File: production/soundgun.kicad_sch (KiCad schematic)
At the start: 16 parts, among them J1 STX-3000, J3 Screw_Terminal_01x02, J4 Screw_Terminal_01x02, U1 LM358, U2 MIC4427, U3 Pico

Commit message: Cleaned Release project
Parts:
- removed J4: Screw_Terminal_01x02, TerminalBlock_Phoenix:TerminalBlock_Phoenix_PT-1,5-2-3.5-H_1x02_P3.50mm_Horizontal, symbol Connector:Screw_Terminal_01x02
- renumbered C6 to C1, D3 to D1, J3 to J2, R4 to R1, R8 to R2, R10 to R3, R9 to R4, R1 to R5
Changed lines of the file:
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@@
 		(dnp no)
 		(fields_autoplaced yes)
-		(property "Reference" "R9"
+		(property "Reference" "R4"
 			(at 140.97 152.4 90)
 			(effects
@@
 			(project "soundgun"
 				(path "/09bb77e0-3bf3-4c24-ad5d-31155c7bb1e6"
-					(reference "R9")
+					(reference "R4")
 					(unit 1)
 				)
@@
 		(dnp no)
 		(fields_autoplaced yes)
-		(property "Reference" "#PWR016"
+		(property "Reference" "#PWR07"
 			(at 273.05 165.1 0)
 			(effects
@@
 			(project "soundgun"
 				(path "/09bb77e0-3bf3-4c24-ad5d-31155c7bb1e6"
-					(reference "#PWR016")
+					(reference "#PWR07")
 					(unit 1)
 				)
@@
 		(dnp no)
 		(fields_autoplaced yes)
-		(property "Reference" "C6"
+		(property "Reference" "C1"
 			(at 105.41 182.8799 0)
 			(effects
@@
 			(project "soundgun"
 				(path "/09bb77e0-3bf3-4c24-ad5d-31155c7bb1e6"
-					(reference "C6")
+					(reference "C1")
 					(unit 1)
 				)
@@
 		(dnp no)
 		(fields_autoplaced yes)
-		(property "Reference" "#PWR025"
+		(property "Reference" "#PWR01"
 			(at 35.56 151.13 0)
 			(effects
@@
 			(project "soundgun"
 				(path "/09bb77e0-3bf3-4c24-ad5d-31155c7bb1e6"
-					(reference "#PWR025")
+					(reference "#PWR01")
 					(unit 1)
 				)
@@
 		(on_board yes)
 		(dnp no)
-		(property "Reference" "#PWR09"
+		(property "Reference" "#PWR05"
 			(at 55.88 152.4 0)
 			(effects
@@
 			(project "soundgun"
 				(path "/09bb77e0-3bf3-4c24-ad5d-31155c7bb1e6"
-					(reference "#PWR09")
+					(reference "#PWR05")
 					(unit 1)
 				)
@@
 		(dnp no)
 		(fields_autoplaced yes)
-		(property "Reference" "R8"
+		(property "Reference" "R2"
 			(at 127 152.4 90)
 			(effects
@@
 			(project "soundgun"
 				(path "/09bb77e0-3bf3-4c24-ad5d-31155c7bb1e6"
-					(reference "R8")
+					(reference "R2")
 					(unit 1)
 				)
@@
 		(dnp no)
 		(fields_autoplaced yes)
-		(property "Reference" "#PWR02"
+		(property "Reference" "#PWR06"
 			(at 80.01 129.54 0)
 			(effects
@@
 			(project "soundgun"
 				(path "/09bb77e0-3bf3-4c24-ad5d-31155c7bb1e6"
-					(reference "#PWR02")
+					(reference "#PWR06")
 					(unit 1)
 				)
@@
 		(dnp no)
 		(fields_autoplaced yes)
-		(property "Reference" "R4"
+		(property "Reference" "R1"
 			(at 110.49 160.0199 0)
 			(effects
@@
 			(project "soundgun"
 				(path "/09bb77e0-3bf3-4c24-ad5d-31155c7bb1e6"
-					(reference "R4")
-					(unit 1)
-				)
-			)
-		)
-	)
-	(symbol
-		(lib_id "Connector:Screw_Terminal_01x02")
-		(at 59.69 168.91 0)
-		(mirror y)
-		(unit 1)
-		(exclude_from_sim no)
-		(in_bom yes)
-		(on_board yes)
-		(dnp no)
-		(property "Reference" "J4"
-			(at 57.15 168.9099 0)
-			(effects
-				(font
-					(size 1.27 1.27)
-				)
-				(justify left)
-			)
-		)
-		(property "Value" "Screw_Terminal_01x02"
-			(at 57.15 171.4499 0)
-			(effects
-				(font
-					(size 1.27 1.27)
-				)
-				(justify left)
-			)
-		)
-		(property "Footprint" "TerminalBlock_Phoenix:TerminalBlock_Phoenix_PT-1,5-2-3.5-H_1x02_P3.50mm_Horizontal"
-			(at 59.69 168.91 0)
-			(effects
-				(font
-					(size 1.27 1.27)
-				)
-				(hide yes)
-			)
-		)
-		(property "Datasheet" "~"
-			(at 59.69 168.91 0)
-			(effects
-				(font
-					(size 1.27 1.27)
-				)
-				(hide yes)
-			)
-		)
-		(property "Description" "Generic screw terminal, single row, 01x02, script generated (kicad-library-utils/schlib/autogen/connector/)"
-			(at 59.69 168.91 0)
-			(effects
-				(font
-					(size 1.27 1.27)
-				)
-				(hide yes)
-			)
-		)
-		(pin "2"
-		)
-		(pin "1"
-		)
-		(instances
-			(project "soundgun"
-				(path "/09bb77e0-3bf3-4c24-ad5d-31155c7bb1e6"
-					(reference "J4")
+					(reference "R1")
 					(unit 1)
 				)
@@
 		(on_board yes)
 		(dnp no)
-		(property "Reference" "R1"
+		(property "Reference" "R5"
 			(at 140.97 166.624 90)
 			(effects
@@
 			(project "soundgun"
 				(path "/09bb77e0-3bf3-4c24-ad5d-31155c7bb1e6"
-					(reference "R1")
+					(reference "R5")
 					(unit 1)
 				)
@@
 		(dnp no)
 		(fields_autoplaced yes)
-		(property "Reference" "#PWR01"
+		(property "Reference" "#PWR04"
 			(at 49.53 130.81 0)
 			(effects
@@
 			(project "soundgun"
 				(path "/09bb77e0-3bf3-4c24-ad5d-31155c7bb1e6"
-					(reference "#PWR01")
+					(reference "#PWR04")
 					(unit 1)
 				)
@@
 		(dnp no)
 		(fields_autoplaced yes)
-		(property "Reference" "R10"
+		(property "Reference" "R3"
 			(at 127 163.83 90)
 			(effects
@@
 			(project "soundgun"
 				(path "/09bb77e0-3bf3-4c24-ad5d-31155c7bb1e6"
-					(reference "R10")
+					(reference "R3")
 					(unit 1)
 				)
@@
 		(dnp no)
 		(fields_autoplaced yes)
-		(property "Reference" "#FLG05"
+		(property "Reference" "#FLG01"
 			(at 25.4 168.275 0)
 			(effects
@@
 			(project "soundgun"
 				(path "/09bb77e0-3bf3-4c24-ad5d-31155c7bb1e6"
-					(reference "#FLG05")
+					(reference "#FLG01")
 					(unit 1)
 				)
@@
 		(dnp no)
 		(fields_autoplaced yes)
-		(property "Reference" "D3"
+		(property "Reference" "D1"
 			(at 157.48 176.8474 90)
 			(effects
@@
 			(project "soundgun"
 				(path "/09bb77e0-3bf3-4c24-ad5d-31155c7bb1e6"
-					(reference "D3")
+					(reference "D1")
 					(unit 1)
 				)
@@
 		(dnp no)
 		(fields_autoplaced yes)
-		(property "Reference" "#PWR010"
+		(property "Reference" "#PWR03"
 			(at 46.99 152.4 0)
 			(effects
@@
 			(project "soundgun"
 				(path "/09bb77e0-3bf3-4c24-ad5d-31155c7bb1e6"
-					(reference "#PWR010")
+					(reference "#PWR03")
 					(unit 1)
 				)
@@
 		(on_board yes)
 		(dnp no)
-		(property "Reference" "J3"
+		(property "Reference" "J2"
 			(at 251.46 133.3501 0)
 			(effects
@@
 			(project "soundgun"
 				(path "/09bb77e0-3bf3-4c24-ad5d-31155c7bb1e6"
-					(reference "J3")
+					(reference "J2")
 					(unit 1)
 				)
@@
 		(dnp no)
 		(fields_autoplaced yes)
-		(property "Reference" "#PWR024"
+		(property "Reference" "#PWR02"
 			(at 35.56 165.1 0)
 			(effects
@@
 			(project "soundgun"
 				(path "/09bb77e0-3bf3-4c24-ad5d-31155c7bb1e6"
-					(reference "#PWR024")
-					(unit 1)
-				)
+					(reference "#PWR02")
+					(unit 1)
+				)

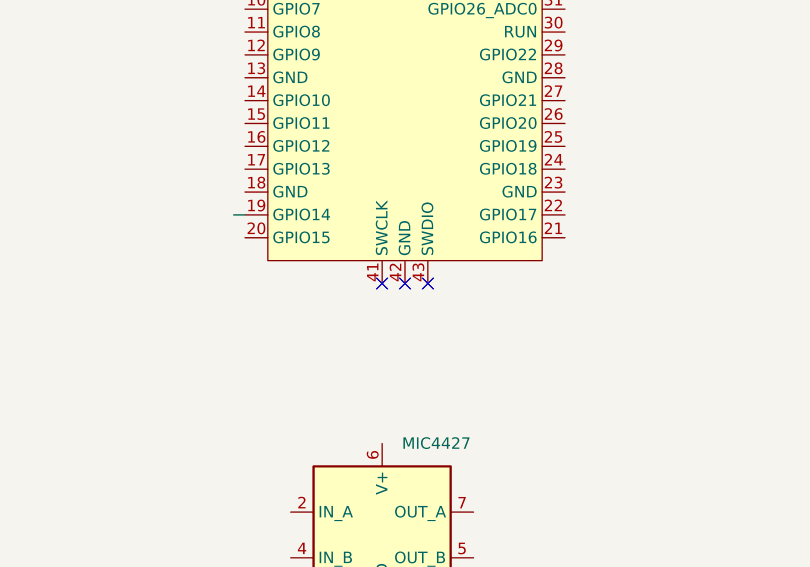
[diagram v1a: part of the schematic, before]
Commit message: Added model paths
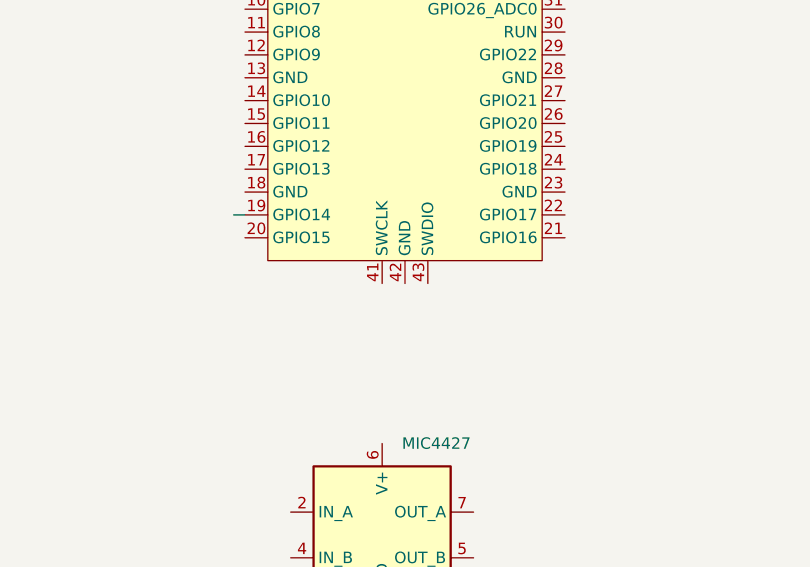
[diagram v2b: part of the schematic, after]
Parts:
- J1: footprint stx3000:STX-3000_KYC -> Connector_stx3000:STX-3000_KYC
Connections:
- no-connect marks 4 -> 1
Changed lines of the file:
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@@
 		(at 68.58 116.84)
-	)
-	(no_connect
-		(at 172.72 104.14)
-	)
-	(no_connect
-		(at 167.64 104.14)
-	)
-	(no_connect
-		(at 170.18 104.14)
 	)
 	(wire
@@
 			)
 		)
-		(property "Footprint" "stx3000:STX-3000_KYC"
+		(property "Footprint" "Connector_stx3000:STX-3000_KYC"
 			(at 57.15 77.47 0)
 			(effects

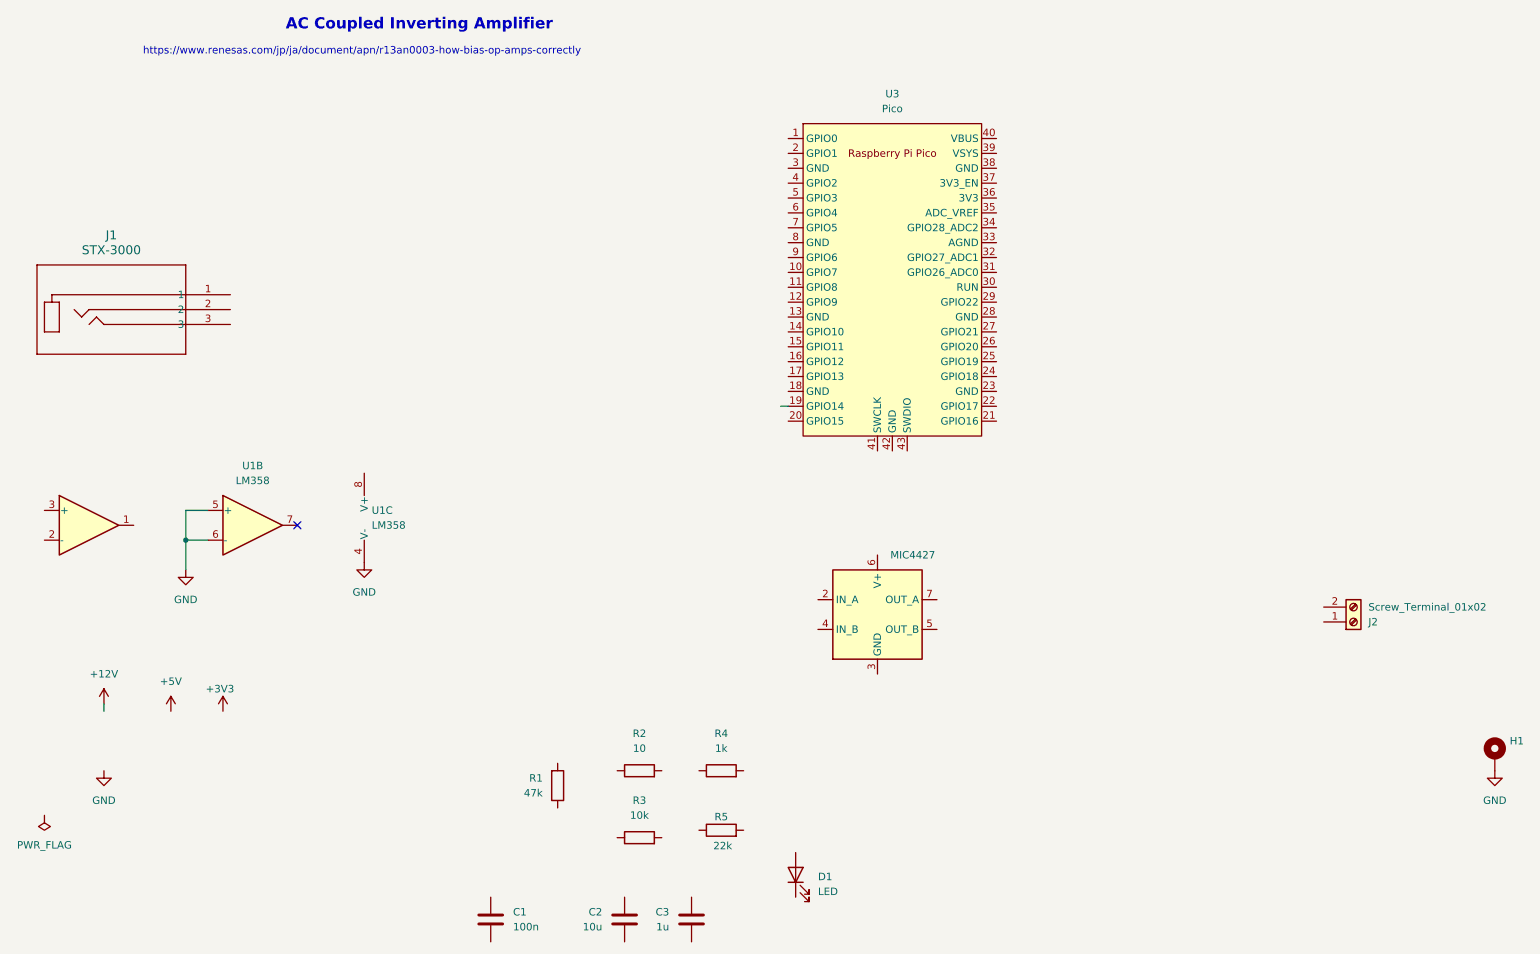
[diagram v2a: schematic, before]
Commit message: Created production PCB
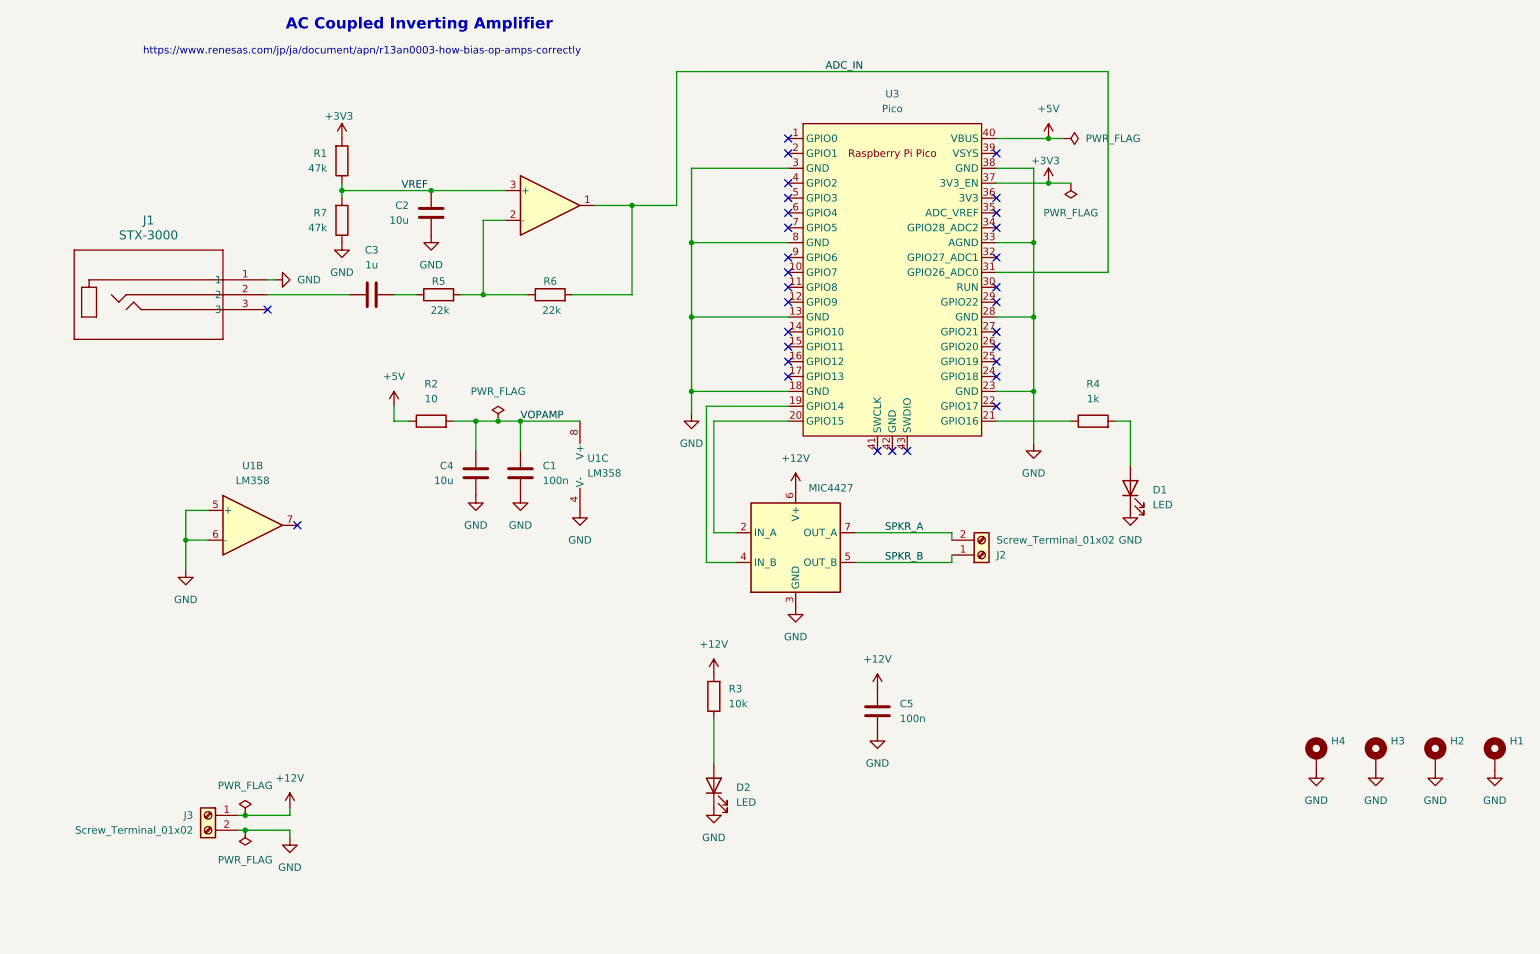
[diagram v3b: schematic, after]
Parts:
- added C4: 10u, Capacitor_THT:C_Disc_D4.7mm_W2.5mm_P5.00mm, symbol Device:C
- added C5: 100n, Capacitor_THT:C_Disc_D3.8mm_W2.6mm_P2.50mm, symbol Device:C
- added D2: LED, LED_THT:LED_D5.0mm, symbol Device:LED
- added H2, H3, H4: MountingHole_Pad, MountingHole:MountingHole_3.2mm_M3_DIN965_Pad, symbol Mechanical:MountingHole_Pad
- added J3: Screw_Terminal_01x02, TerminalBlock_Phoenix:TerminalBlock_Phoenix_PT-1,5-2-3.5-H_1x02_P3.50mm_Horizontal, symbol Connector:Screw_Terminal_01x02
- added R6: 22k, Resistor_THT:R_Axial_DIN0204_L3.6mm_D1.6mm_P7.62mm_Horizontal, symbol Device:R
- added R7: 47k, Resistor_THT:R_Axial_DIN0204_L3.6mm_D1.6mm_P7.62mm_Horizontal, symbol Device:R
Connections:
- net +12V: now also R3.2, U2.6 (V+), C5.2, J3.1 (Pin_1)
- net +3V3: now also R1.2, U3.37 (3V3_EN)
- net +5V: now also R2.1, U3.40 (VBUS)
- net GND: now also C1.1, C2.1, D1.1 (K), J1.1, U2.3 (GND), U3.13 (GND), U3.18 (GND), U3.23 (GND), U3.28 (GND), U3.3 (GND), U3.33 (AGND), U3.38 (GND), U3.8 (GND), C4.1, C5.1, D2.1 (K), H2.1, H3.1, H4.1, J3.2 (Pin_2), R7.1
- net at R4.1: now also U3.21 (GPIO16)
- net at R4.2: now also D1.2 (A)
- net at U2.2 (IN_A): now also U3.20 (GPIO15)
- net at U2.4 (IN_B): now also U3.19 (GPIO14)
- net SPKR_B: now reaches U2.5 (OUT_B)
- net SPKR_B: now also J2.1 (Pin_1)
- net SPKR_A: now reaches U2.7 (OUT_A)
- net SPKR_A: now also J2.2 (Pin_2)
- net at J1.2: now also C3.1
- net VOPAMP: now reaches C1.2
- net VOPAMP: now also R2.2, U1.8 (V+), C4.2
- net VREF: now reaches C2.2
- net VREF: now also R1.1, U1.3 (+), R7.2
- net ADC_IN: now reaches U3.31 (GPIO26_ADC0)
- net ADC_IN: now also U1.1, R6.2
- net at C3.2: now also R5.1
- net at R5.2: now also U1.2 (-), R6.1
- net at R3.1: now also D2.2 (A)
- no-connect marks 1 -> 31
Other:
- moved on the sheet: C1, C2, C3, D1, J1, J2, R1, R2, R3, R4, R5, U1C
